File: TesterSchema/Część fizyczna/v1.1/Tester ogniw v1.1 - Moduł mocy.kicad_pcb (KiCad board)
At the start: 2 copper layers, 182 x 75 mm, 42 parts, among them J1 J2, K1 K10, K3 Zasilanie, K4 Badany AKU, T1 IRFP9140, T2 IRFP054N, T3 BC547, T4 BC547, T5 T_PNP, T6 BC547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

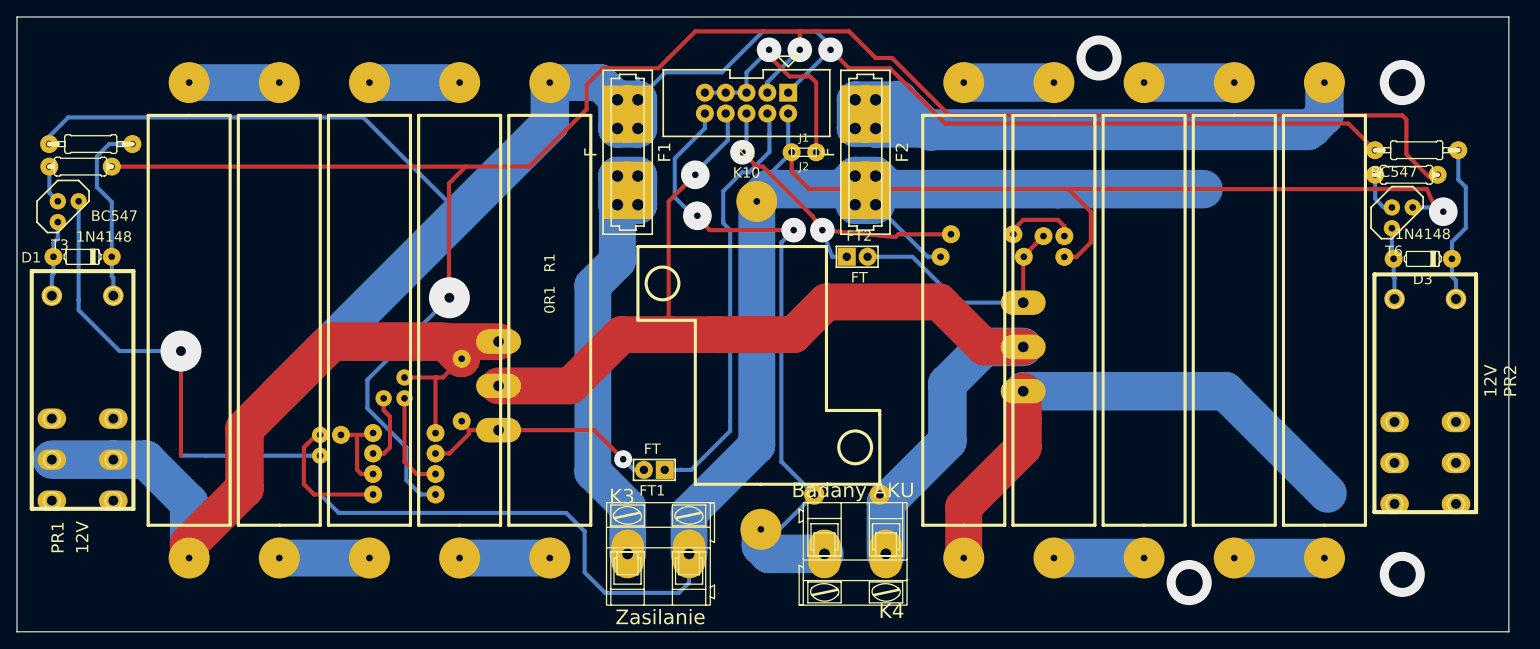
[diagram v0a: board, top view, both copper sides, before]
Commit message: dodanie brakujących ściażek do modułu wykonawczego
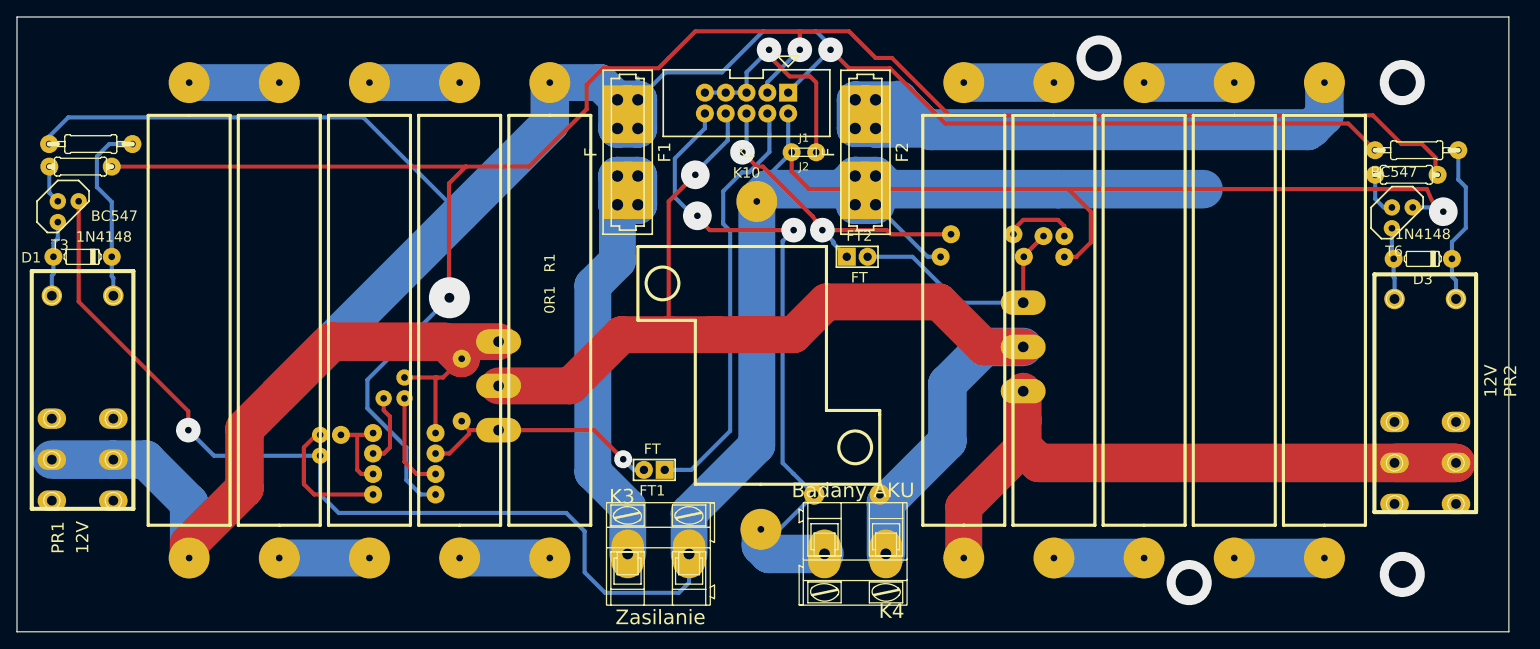
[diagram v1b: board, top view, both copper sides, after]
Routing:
- net N-0000030: track 65.7 -> 84.4 mm
- net GND: track 356.1 -> 348.2 mm
- net /NoDAC: track 239.4 -> 238.3 mm
- net /DSG: track 39.9 -> 39.2 mm
- net N-0000029: track 130.4 -> 129.8 mm
